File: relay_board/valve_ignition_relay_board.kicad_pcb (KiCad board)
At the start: 4 copper layers, 63.8 x 103.9 mm, 92 parts, among them J1 Programming Header, J2 ACT_PWR, J3 ACT_PWR, J4 Actuator, J5 CAN Connector Left, J6 CAN Connector Right, K1 PS2702-1-F3-A, K2 PS2702-1-F3-A, K3 T9GV1L14-12, K4 T92S11D12-12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

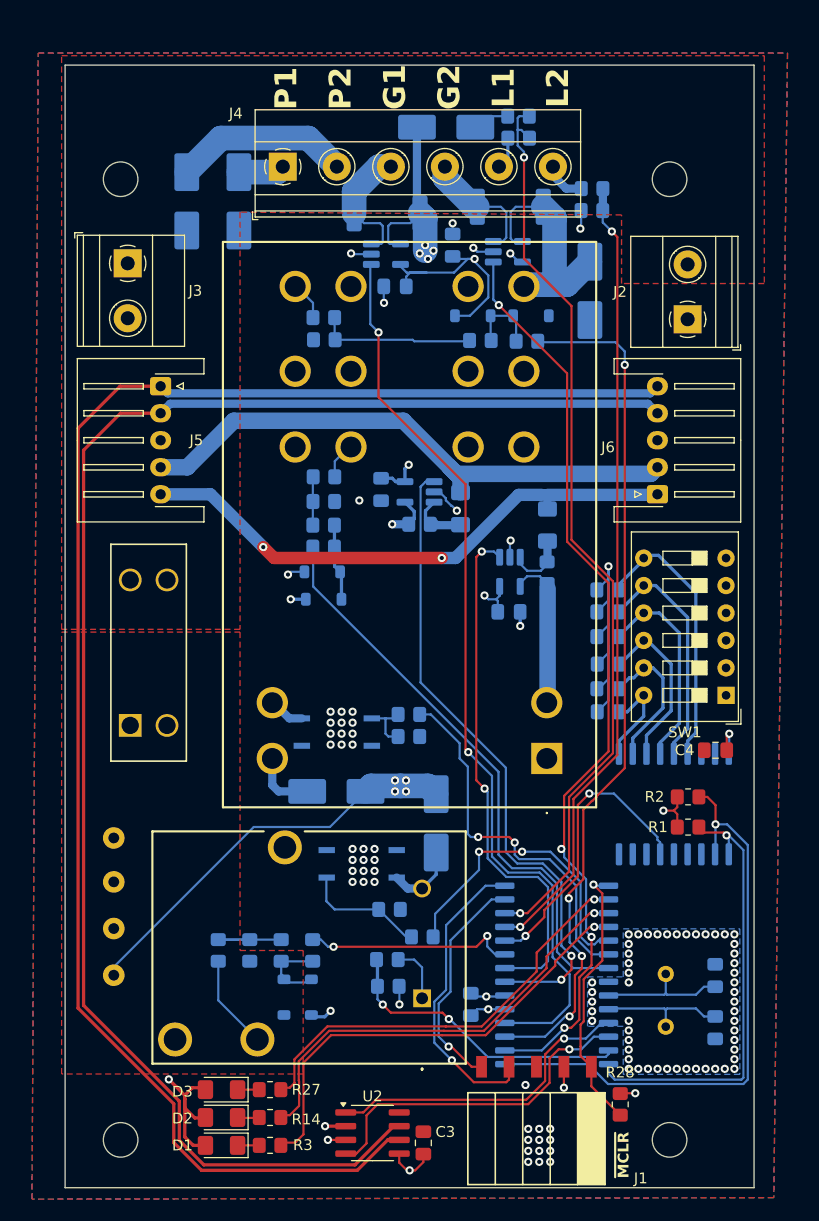
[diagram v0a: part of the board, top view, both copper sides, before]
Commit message: lowpass current sense; move power traces to FCu
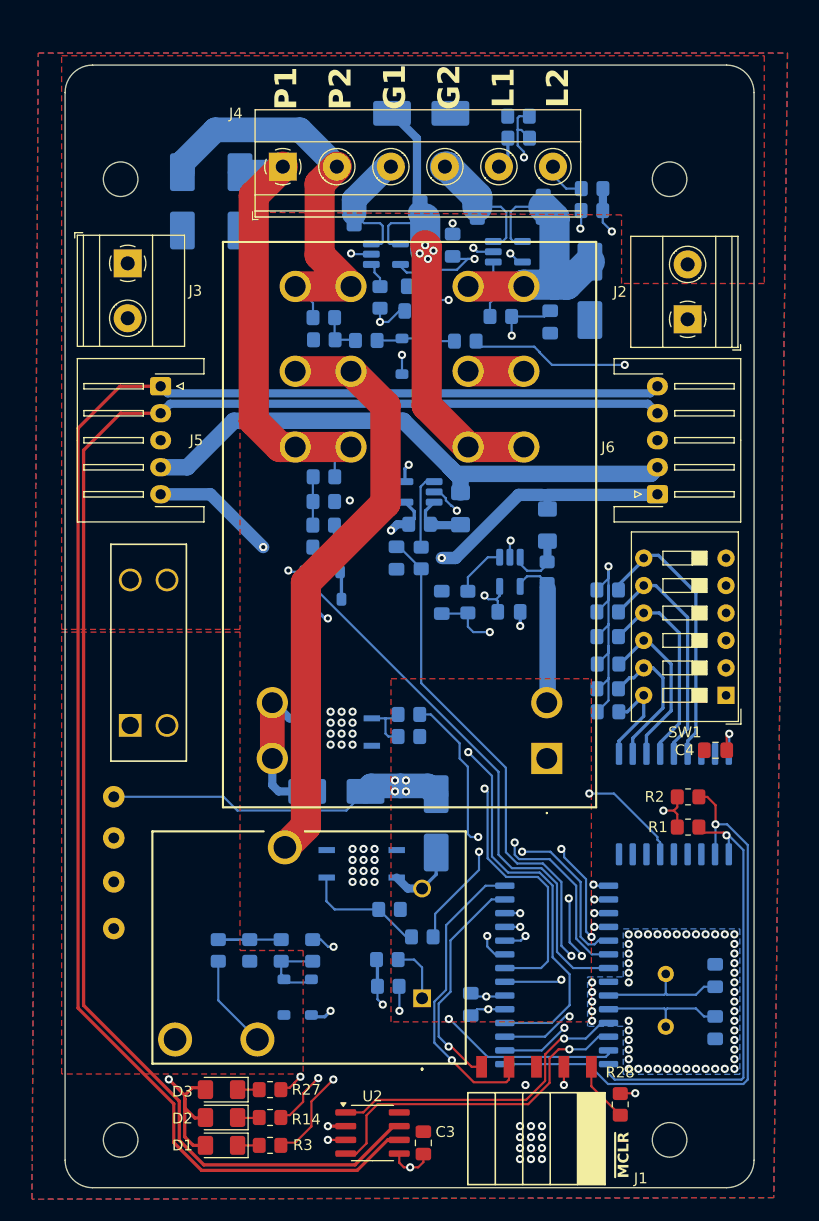
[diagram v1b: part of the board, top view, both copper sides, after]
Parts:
- added C10: 1.6nF, Capacitor_SMD:C_0805_2012Metric_Pad1.18x1.45mm_HandSolder, B.Cu at (127.0, 48.8)
- added C11: 1.6nF, Capacitor_SMD:C_0805_2012Metric_Pad1.18x1.45mm_HandSolder, B.Cu at (139.4, 49.8)
- added C12: 1.6nF, Capacitor_SMD:C_0805_2012Metric_Pad1.18x1.45mm_HandSolder, B.Cu at (129.4, 75.7)
- added C13: 1.6nF, Capacitor_SMD:C_0805_2012Metric_Pad1.18x1.45mm_HandSolder, B.Cu at (125.2, 71.6)
- added R30: 500R, Resistor_SMD:R_0805_2012Metric_Pad1.20x1.40mm_HandSolder, B.Cu at (123.7, 47.5)
- added R31: 500R, Resistor_SMD:R_0805_2012Metric_Pad1.20x1.40mm_HandSolder, B.Cu at (134.9, 49.3)
- added R32: 500R, Resistor_SMD:R_0805_2012Metric_Pad1.20x1.40mm_HandSolder, B.Cu at (131.8, 75.7)
- added R33: 500R, Resistor_SMD:R_0805_2012Metric_Pad1.20x1.40mm_HandSolder, B.Cu at (127.5, 71.6)
- R29: value 0.25 -> 0.25R
- moved TP3 16.5 mm to (99.1, 93.7)
- moved R39 10.6 mm to (122.4, 51.5)
- moved D10 10.2 mm to (128.3, 53.1), turned to -90 degrees
- moved D11 7.55 mm to (125.7, 53.0), turned to 90 degrees
- moved R41 5.71 mm to (131.6, 51.6)
- moved D6 2.64 mm to (127.5, 30.5)
- moved C5 2.17 mm to (127.3, 46.5)
- moved D9 0.40 mm to (105.4, 38.6)
- moved D8 0.11 mm to (110.7, 38.6)
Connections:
- U10 pad 1: /DipSwitch/CURRSENSE_IN5V -> Net-(U10-VO)
- U11 pad 1: /DipSwitch/CURRSENSE_IN12V -> Net-(U11-VO)
- U7 pad 1: /DipSwitch/CURR_SENSE_2 -> Net-(U7-VO)
- U8 pad 1: /DipSwitch/CURR_SENSE_1 -> Net-(U8-VO)
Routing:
- net +12V: track 100.6 -> 52.5 mm
- net /DipSwitch/VSENSE_OUTPUT2: track 14.6 -> 3.98 mm
- net Net-(U10-VO): track 0.00 -> 7.07 mm
- net +5V: track 96.3 -> 89.9 mm, vias 16 -> 17
- net /DipSwitch/CURRSENSE_IN5V: track 59.9 -> 54.0 mm
- net Net-(U7-VO): track 0.00 -> 5.17 mm
- net Net-(U11-VO): track 0.00 -> 5.01 mm
- net Net-(U9-RC6): track 80.4 -> 85.4 mm
- net /DipSwitch/CURRSENSE_IN12V: track 48.7 -> 45.7 mm
- net Net-(U9-RA2): track 42.7 -> 40.2 mm, vias 1 -> 2
- net Net-(U8-VO): track 0.00 -> 2.52 mm
- net /Relay/T92S11D12-12/NC2: track 43.4 -> 45.6 mm
- net Net-(U9-RA1): track 41.2 -> 39.2 mm, vias 1 -> 2
- net /Relay/P2: track 37.9 -> 39.7 mm
- net /Relay/P1: track 40.7 -> 42.3 mm
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- added copper zone on F.Cu, net +12V
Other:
- outline, holes or cut-outs redrawn
